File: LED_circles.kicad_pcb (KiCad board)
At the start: 2 copper layers, 125 x 125 mm, 134 parts, among them J1 Conn_ARM_SWD_EDGE, J2 USB4125-GF-A, U74 BD33GA3WEFJ, U75 M95256-WMN6P, U76 M95256-WMN6P, U77 STM32G071KBTxN

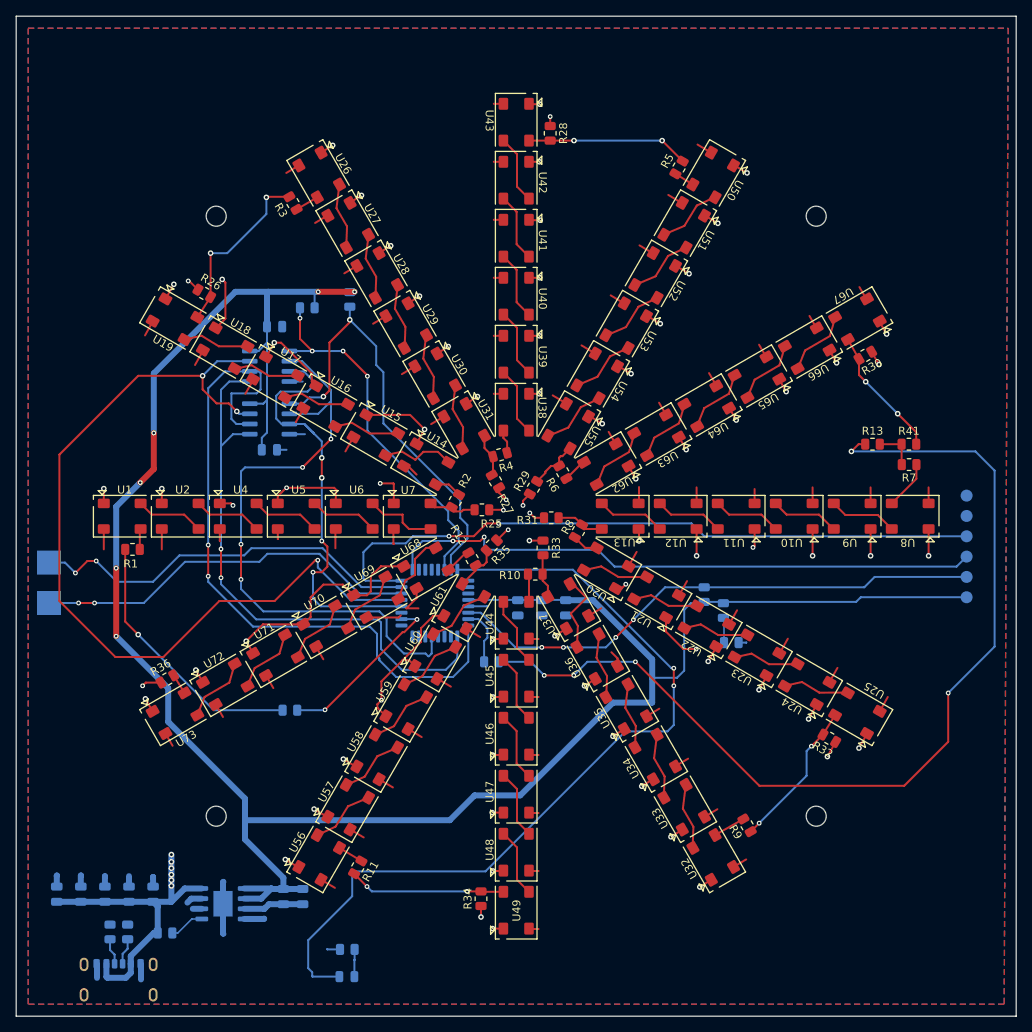
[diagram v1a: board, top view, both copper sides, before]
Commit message: Deleted parts not used in single row test PCB
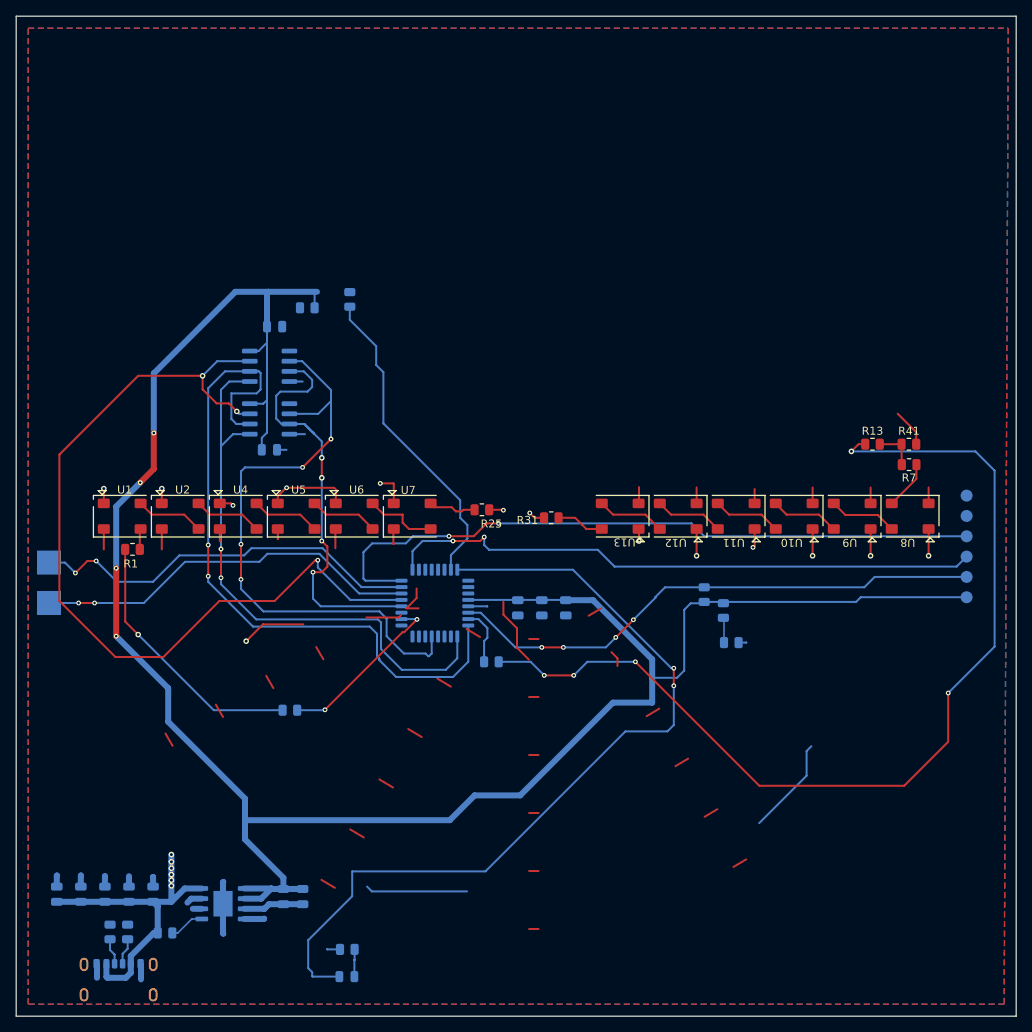
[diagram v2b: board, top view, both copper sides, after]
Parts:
- removed H1, H2, H3, H4: MountingHole, MountingHole:MountingHole_2.5mm
- removed R10, R11, R12, R2, R26, R27, R28, R29, R3, R30, R32, R33, R34, R35, R36, R4, R5, R6, R8, R9: 0, Resistor_SMD:R_0805_2012Metric
- removed U14, U15, U16, U17, U18, U19, U20, U21, U22, U23, U24, U25, U26, U27, U28, U29, U30, U31, U32, U33, U34, U35, U36, U37, U38, U39, U40, U41, U42, U43, U44, U45, U46, U47, U48, U49, U50, U51, U52, U53, U54, U55, U56, U57, U58, U59, U60, U61, U62, U63, U64, U65, U66, U67, U68, U69, U70, U71, U72, U73: ~, LED_circles_footprints:IN-PI55TAT
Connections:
- R41 pad 2: /Row6/DOUT_{TOP} -> /Row1/DOUT_{TOP}
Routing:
- net GND: track 259.8 -> 89.1 mm, vias 76 -> 14
- net +5V: track 176.0 -> 111.1 mm
- net /LED_circles_ucontroller/EEPROM2_CS: track 46.8 -> 0.00 mm, vias 4 -> 0
- net (no net): track 0.00 -> 33.6 mm
- net /Row2/DOUT_{TOP}: track 22.5 -> 0.00 mm, vias 2 -> 0
- net /Row4/DOUT_{TOP}: track 20.3 -> 0.00 mm, vias 2 -> 0
- net /Row4/DOUT_{BOTTOM}: track 19.5 -> 0.00 mm, vias 2 -> 0
- net /Row2/DOUT_{BOTTOM}: track 18.7 -> 0.00 mm, vias 2 -> 0
- net /Row6/DOUT_{TOP}: track 16.4 -> 0.00 mm, vias 2 -> 0
- net /LED_circles_ucontroller/EEPROM1_CS: track 55.4 -> 39.8 mm, vias 2 -> 0
- net Net-(U36-DOUT): track 9.71 -> 0.00 mm
- net Net-(U14-DOUT): track 9.24 -> 0.00 mm
- net Net-(U68-DOUT): track 8.97 -> 0.00 mm
- net Net-(U45-DOUT): track 8.58 -> 0.00 mm
- net Net-(U46-DOUT): track 8.58 -> 0.00 mm
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
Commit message: Shrunk board outline to 94mm x 75mm
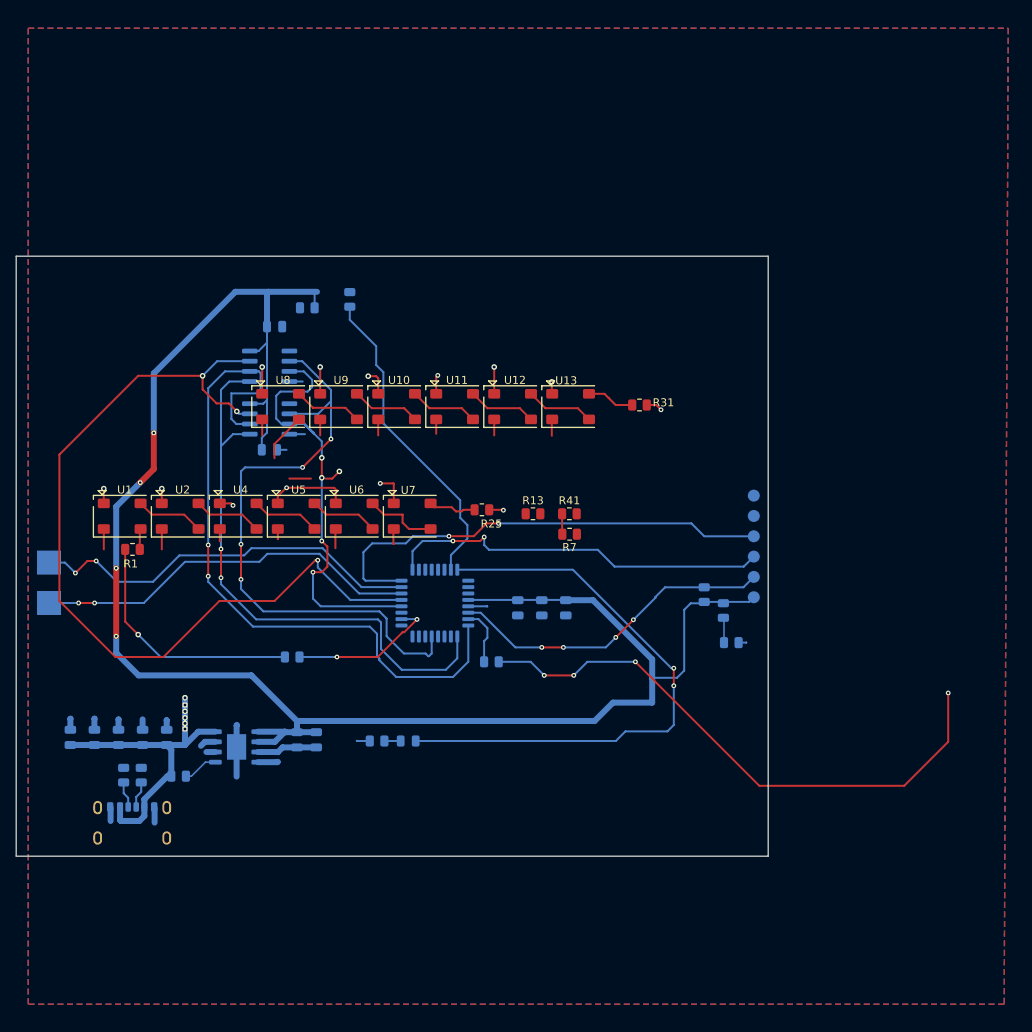
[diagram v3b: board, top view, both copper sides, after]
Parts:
- moved U8 79.9 mm to (114.0, 86.3), turned to 0 degrees
- moved U9 65.6 mm to (121.3, 86.3), turned to 0 degrees
- moved U10 51.6 mm to (128.6, 86.3), turned to 0 degrees
- moved R13 43.3 mm to (145.6, 99.7)
- moved R41 43.3 mm to (150.2, 99.7)
- moved R7 43.3 mm to (150.2, 102.2)
- moved U11 37.8 mm to (135.8, 86.3), turned to 0 degrees
- moved D1 30.4 mm to (130.0, 128.1), turned to 0 degrees
- moved J1 26.6 mm to (173.2, 103.8)
- moved R48 26.3 mm to (126.1, 128.1)
- moved U12 24.8 mm to (143.1, 86.3), turned to 0 degrees
- moved C6 19.7 mm to (116.1, 128.0)
- moved C7 19.7 mm to (118.5, 128.0)
- moved C1 19.7 mm to (99.8, 127.7)
- moved C2 19.7 mm to (96.8, 127.7)
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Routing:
- net /LED_circles_ucontroller/BOTTOM_ROWS: track 123.6 -> 74.5 mm
- net +3.3V: track 276.8 -> 227.9 mm
- net +5V: track 111.1 -> 64.8 mm
- net Net-(D1-A): track 106.0 -> 72.4 mm
- net (no net): track 33.6 -> 0.00 mm
- net /LED_circles_ucontroller/SWCLK-BOOT0: track 75.0 -> 48.4 mm
- net Net-(J1-~{RESET}): track 67.8 -> 41.2 mm
- net /LED_circles_ucontroller/SWDIO: track 85.7 -> 59.1 mm
- net GND: track 89.1 -> 81.0 mm, vias 14 -> 13
- net /Row1/DOUT_{TOP}: track 10.8 -> 6.00 mm
- net Net-(U77-PA8): track 21.6 -> 18.6 mm
- net /LED_circles_ucontroller/TOP_ROWS: track 33.3 -> 30.8 mm
- net Net-(D1-K): track 3.41 -> 2.04 mm
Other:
- board size 125 x 125 mm -> 94 x 75 mm

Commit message: Made vias really big so one can make them on a circuit mill
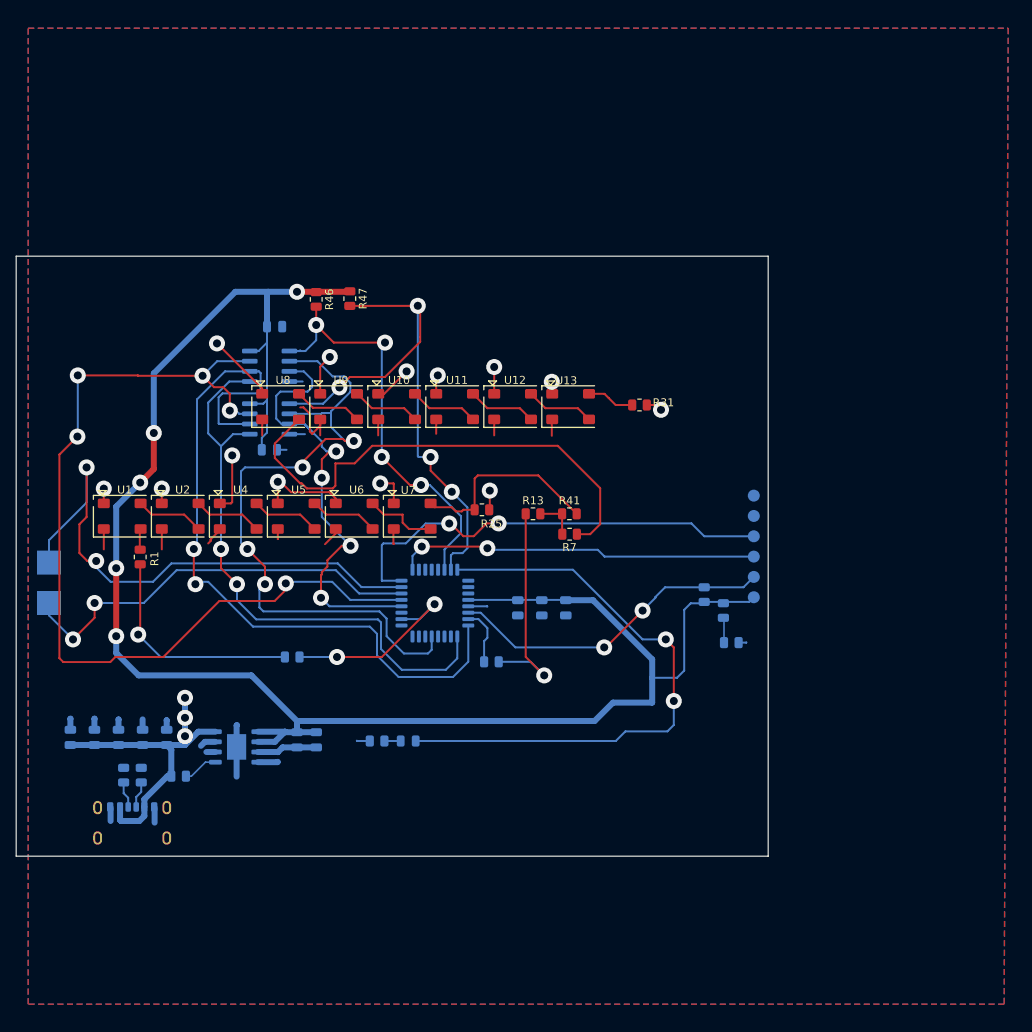
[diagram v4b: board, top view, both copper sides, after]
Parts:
- R46, R47: moved to F.Cu
- moved R46 1.53 mm to (118.5, 72.9), turned to -90 degrees
- moved R1 1.35 mm to (96.5, 105.1), turned to 90 degrees
- moved R47 0.10 mm to (122.7, 72.8)
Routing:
- net Net-(U8-DIN): track 6.12 -> 62.3 mm
- net /LED_circles_ucontroller/EEPROM2_CS: track 0.00 -> 54.0 mm, vias 0 -> 4
- net /LED_circles_ucontroller/BOTTOM_ROWS: track 74.5 -> 27.5 mm, vias 5 -> 1
- net /LED_circles_ucontroller/EEPROM1_CS: track 39.8 -> 70.7 mm, vias 0 -> 4
- net /LED_circles_ucontroller/RX: track 50.1 -> 69.3 mm
- net /Row1/DOUT_{TOP}: track 6.00 -> 24.8 mm
- net GND: track 81.0 -> 96.7 mm
- net /LED_circles_ucontroller/SPI1_MISO: track 77.2 -> 86.0 mm
- net /LED_circles_ucontroller/HOLD: track 109.1 -> 116.4 mm, vias 3 -> 5
- net +5V: track 64.8 -> 71.9 mm, vias 6 -> 3
- net Net-(U77-PA8): track 18.6 -> 24.5 mm
- net /LED_circles_ucontroller/SPI1_SCK: track 87.9 -> 93.8 mm
- net /LED_circles_ucontroller/TX: track 48.7 -> 52.7 mm
- net /LED_circles_ucontroller/WRITE_PROTECT: track 53.4 -> 57.0 mm
- net /LED_circles_ucontroller/SWCLK-BOOT0: track 48.4 -> 45.4 mm
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
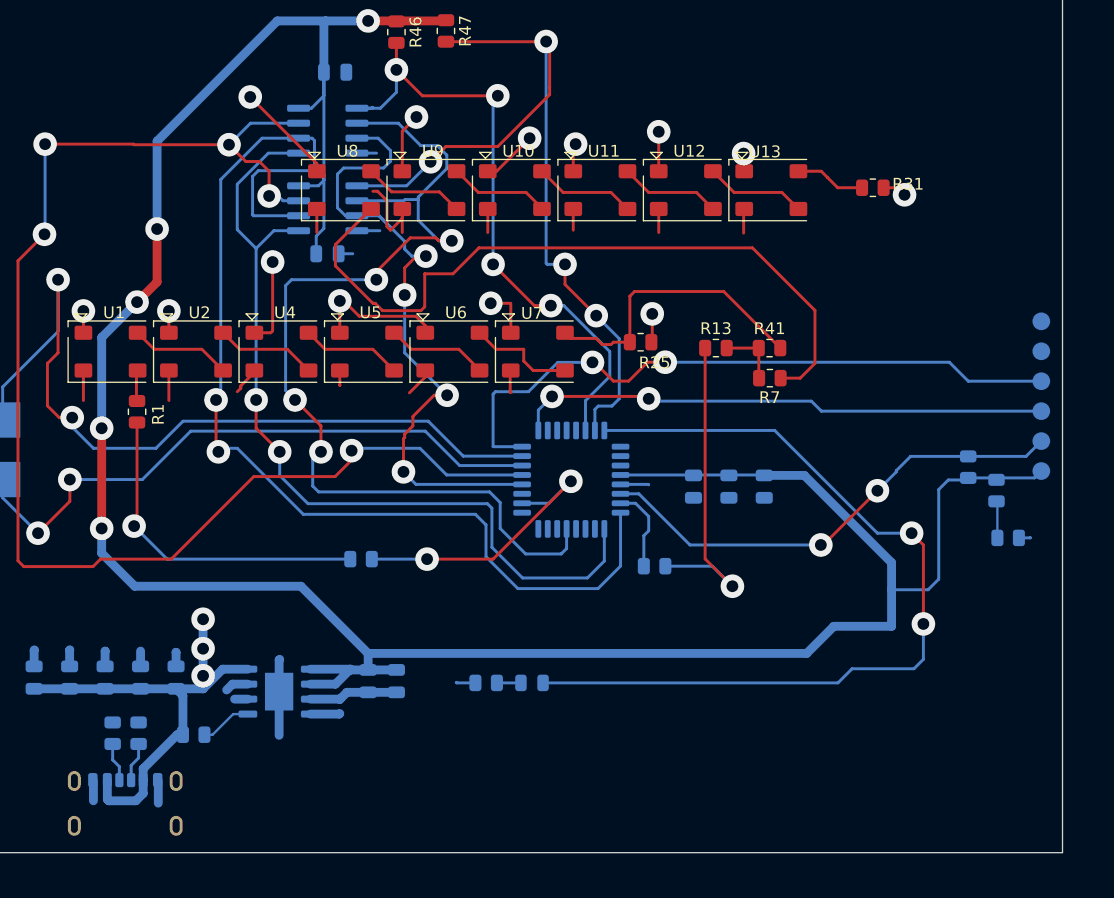
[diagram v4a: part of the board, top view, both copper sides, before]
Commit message: Changed plane thermal relief to use normal traces
This aids in manufacturability on a PCB mill.  You only need to mill out one trace instead of thermal spokes.
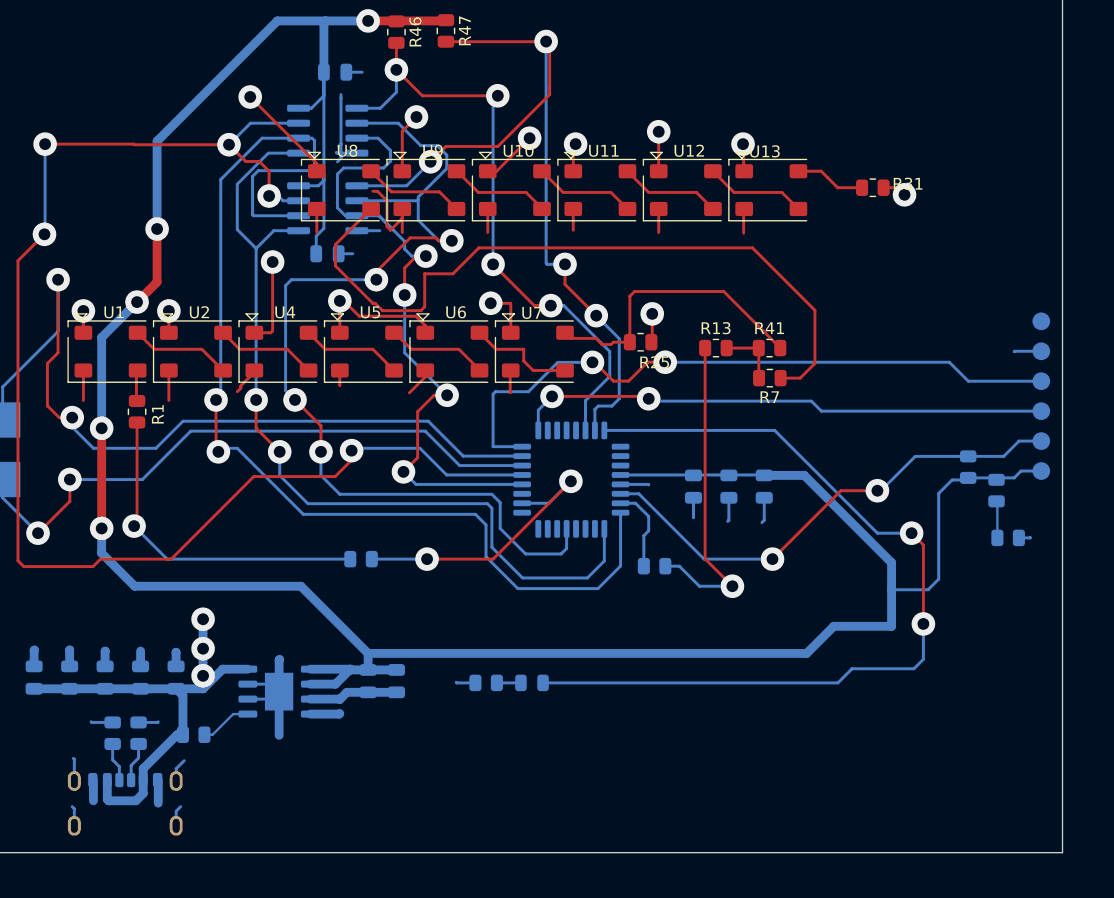
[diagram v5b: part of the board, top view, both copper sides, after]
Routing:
- net GND: track 96.7 -> 127.3 mm
- net /LED_circles_ucontroller/SPI1_MISO: track 86.0 -> 84.4 mm
- net /LED_circles_ucontroller/EEPROM2_CS: track 54.0 -> 52.6 mm
- net Net-(J1-~{RESET}): track 41.2 -> 42.1 mm

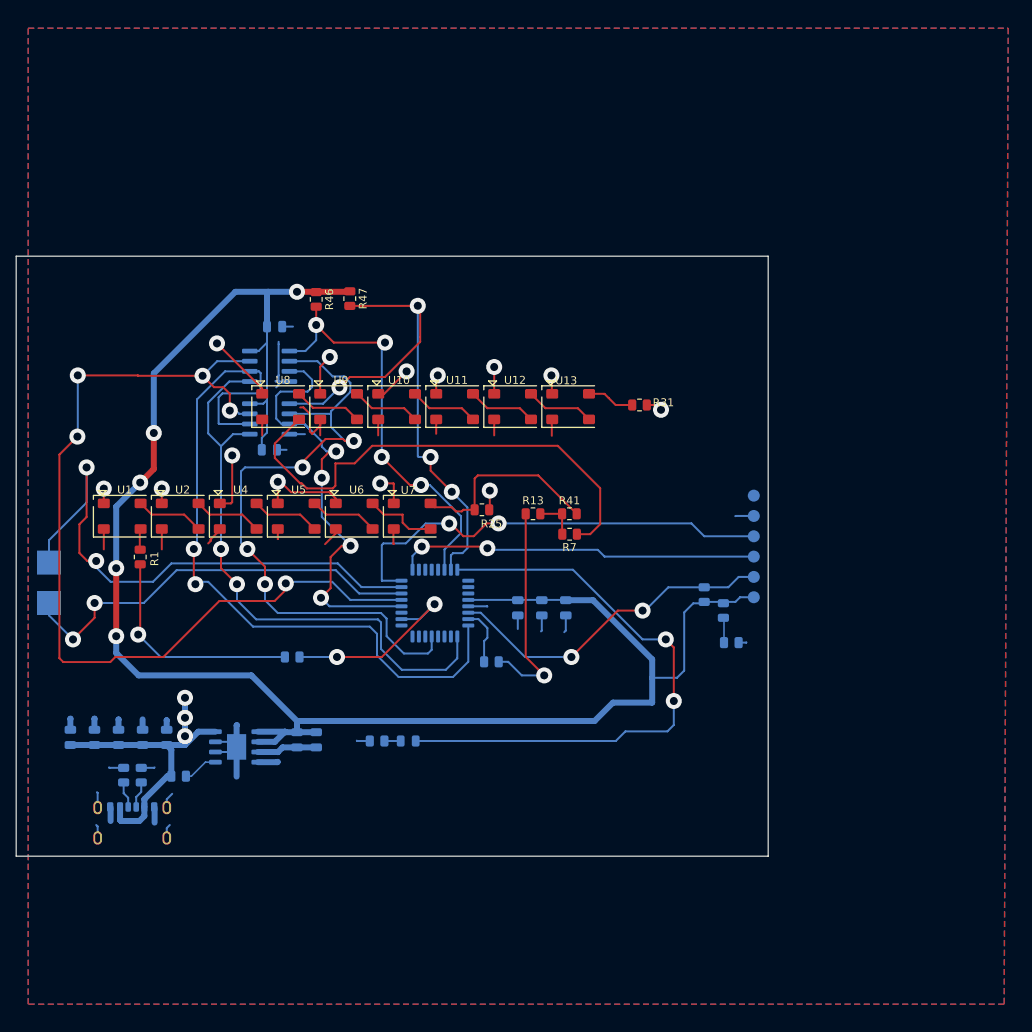
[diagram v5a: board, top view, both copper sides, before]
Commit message: Increased track width
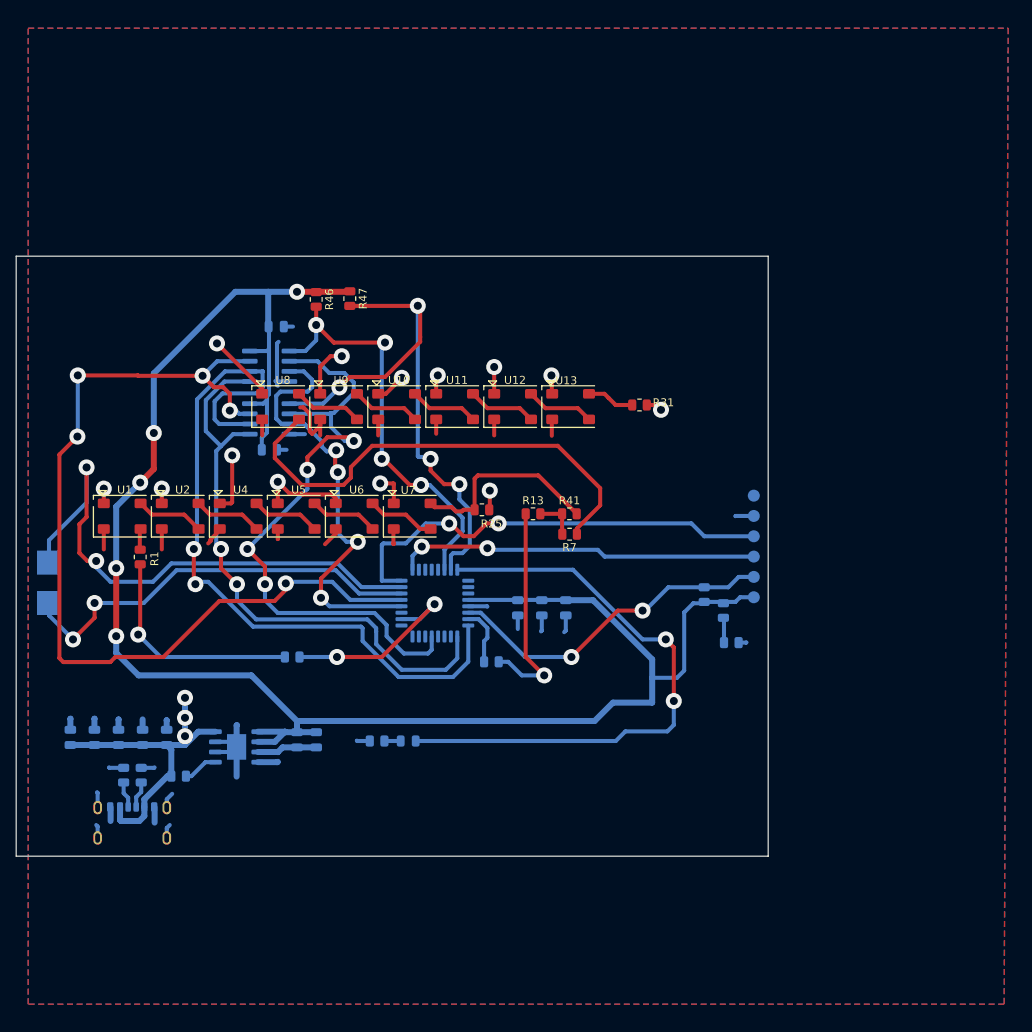
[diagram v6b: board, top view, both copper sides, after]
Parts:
- U1: value ~ -> IN-PI55TAT
- moved C12 0.20 mm to (113.5, 76.3)
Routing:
- net /LED_circles_ucontroller/SPI1_MISO: track 84.4 -> 80.1 mm
- net Net-(U8-DIN): track 62.3 -> 60.1 mm
- net /LED_circles_ucontroller/EEPROM1_CS: track 70.7 -> 71.9 mm
- net +3.3V: track 229.8 -> 228.7 mm
- net /LED_circles_ucontroller/WRITE_PROTECT: track 57.0 -> 56.3 mm
- net Net-(U6-DOUT): track 9.16 -> 8.58 mm

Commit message: WIP
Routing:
- net Net-(U8-DIN): track 60.1 -> 65.4 mm
- net GND: track 127.2 -> 129.5 mm
- net +5V: track 71.9 -> 70.0 mm
- net /Row1/DOUT_{TOP}: track 24.8 -> 26.6 mm
- net /LED_circles_ucontroller/SPI1_MISO: track 80.1 -> 79.1 mm
- net Net-(J1-~{RESET}): track 42.1 -> 42.8 mm
- net /LED_circles_ucontroller/WRITE_PROTECT: track 56.3 -> 56.7 mm, vias 4 -> 2
